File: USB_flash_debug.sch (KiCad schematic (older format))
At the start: 31 parts, among them IC2 TPS7A0518PDBVT, J6 E8124-015-01, J9 E8124-015-01, Q7 BSS138-7-F, Q8 BSS138-7-F, SW1 1X03, U13 FT232RQ-REEL, U9 FSUSB30UMX

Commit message: Routed USB flash and both USB connectors differential signals with tuning
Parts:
- removed U9: FSUSB30UMX, sc606-baseboard-footprints:UMLP-10_1.8x1.4mm, symbol sc606-baseboard:FSUSB30UMX
- added U9: FSUSB30MUX, antmicro-footprints:MSOP-10_W3mm, symbol antmicroInterfaceAnalogSwitchesSpecialPurpose:FSUSB30MUX
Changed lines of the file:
@@
 	14350 5500 14800 5500
-$Comp
-L sc606-baseboard:FSUSB30UMX U?
-U 1 1 62A45764
-P 2100 4650
-AR Path="/63348E64/62A45764" Ref="U?"  Part="1"
-AR Path="/61F60810/62A45764" Ref="U9"  Part="1"
-F 0 "U9" H 2050 5653 60  0000 C CNN
-F 1 "FSUSB30UMX" H 2050 5547 60  0000 C CNN
-F 2 "sc606-baseboard-footprints:UMLP-10_1.8x1.4mm" H 2250 4840 60  0001 L CNN
-F 3 "https://rocelec.widen.net/view/pdf/reufmpzzmy/ONSM-S-A0003587650-1.pdf?t.download=true&u=5oefqw" H 2250 4940 60  0001 L CNN
-F 4 "FSUSB30UMX" H 2250 5140 60  0001 L CNN "MPN"
-F 5 "ON SEMI" H 2270 5750 60  0001 L CNN "Manufacturer"
-	1    2100 4650
-	1    0    0    -1
-$EndComp
 $Comp
 L sc606-baseboard:E8124-015-01 J?
@@
 	1    0    0    -1
 $EndComp
+$Comp
+L antmicroInterfaceAnalogSwitchesSpecialPurpose:FSUSB30MUX U9
+U 1 1 6214D265
+P 2100 4650
+F 0 "U9" H 2050 5653 60  0000 C CNN
+F 1 "FSUSB30MUX" H 2050 5547 60  0000 C CNN
+F 2 "antmicro-footprints:MSOP-10_W3mm" H 2250 4840 60  0001 L CNN
+F 3 "" H 2250 4940 60  0001 L CNN
+F 4 "FSUSB30MUX" H 2250 5140 60  0001 L CNN "MPN"
+F 5 "ON SEMI" H 2270 5750 60  0001 L CNN "Manufacturer"
+	1    2100 4650
+	1    0    0    -1
+$EndComp

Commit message: Connected SIM, SD, SoM GNDs
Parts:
- U9: footprint antmicro-footprints:MSOP-10_W3mm -> sc606-baseboard-footprints:MSOP-10_W3mm; symbol antmicroInterfaceAnalogSwitchesSpecialPurpose:FSUSB30MUX -> sc606-baseboard:FSUSB30MUX
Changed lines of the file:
@@
 $EndComp
 $Comp
-L antmicroInterfaceAnalogSwitchesSpecialPurpose:FSUSB30MUX U9
+L sc606-baseboard:FSUSB30MUX U9
 U 1 1 6214D265
 P 2100 4650
 F 0 "U9" H 2050 5653 60  0000 C CNN
 F 1 "FSUSB30MUX" H 2050 5547 60  0000 C CNN
-F 2 "antmicro-footprints:MSOP-10_W3mm" H 2250 4840 60  0001 L CNN
+F 2 "sc606-baseboard-footprints:MSOP-10_W3mm" H 2250 4840 60  0001 L CNN
 F 3 "" H 2250 4940 60  0001 L CNN
 F 4 "FSUSB30MUX" H 2250 5140 60  0001 L CNN "MPN"

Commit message: All routes connected
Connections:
- net DEBUG_UART_TX: now also D23.1 (CH1), D23.10 (CH1); no longer D23.4 (CH3), D23.7 (CH3)
- new net: D23.4 (CH3), D23.7 (CH3)
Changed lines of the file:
@@
 Text GLabel 14250 5500 0    50   Input ~ 0
 DEBUG_UART_RX
-Text GLabel 14250 5400 0    50   Input ~ 0
+Text GLabel 14250 5200 0    50   Input ~ 0
 DEBUG_UART_TX
 Text GLabel 13900 4000 2    50   Input ~ 0
@@
 $EndComp
 Wire Wire Line
-	14250 5400 14450 5400
+	14250 5200 14450 5200
 Wire Wire Line
 	14250 5500 14350 5500
 Wire Wire Line
-	14450 4850 14450 5400
-Connection ~ 14450 5400
-Wire Wire Line
-	14450 5400 14800 5400
+	14450 4850 14450 5200
+Wire Wire Line
+	14450 5200 14800 5200
 Wire Wire Line
 	14350 4750 14350 5500
@@
 	1    0    0    -1
 $EndComp
+Connection ~ 14450 5200
 $EndSCHEMATC

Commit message: Cleaned/fixed USB flash debug sch
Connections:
- wire segments 115 -> 172
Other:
- note added: "SoM flashing and debug connectors"
- note added: "USB SoM flashing IF"
- note removed: "Micro USB flashing"
- moved on the sheet: C108, C109, C110, C111, C112, C113, C114, C115, C116, C117, C142, C143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

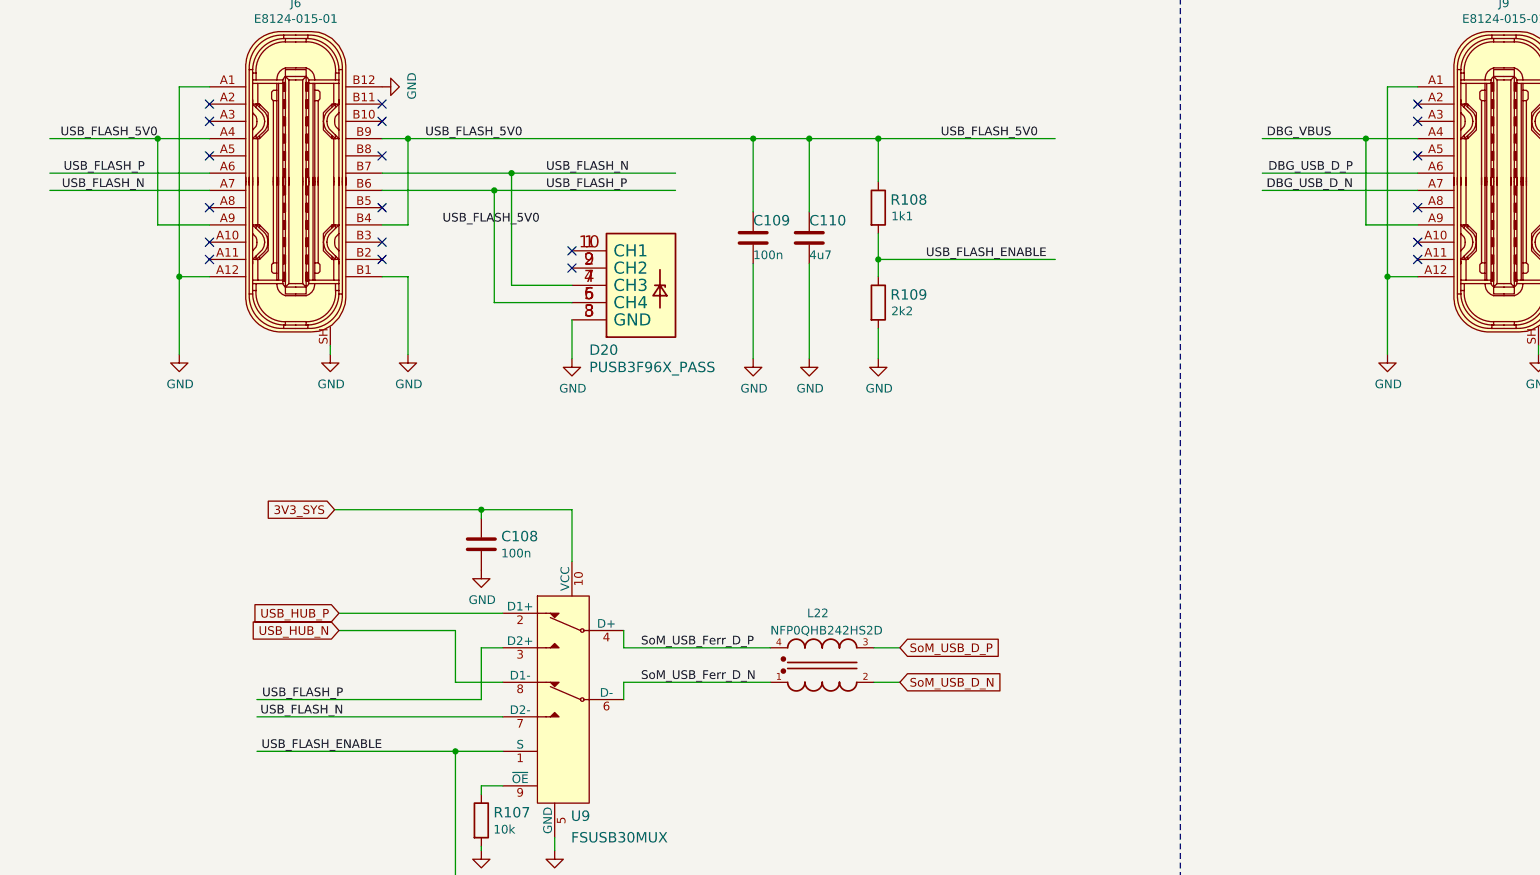
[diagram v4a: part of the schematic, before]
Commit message: Added schema for serial interface connectors
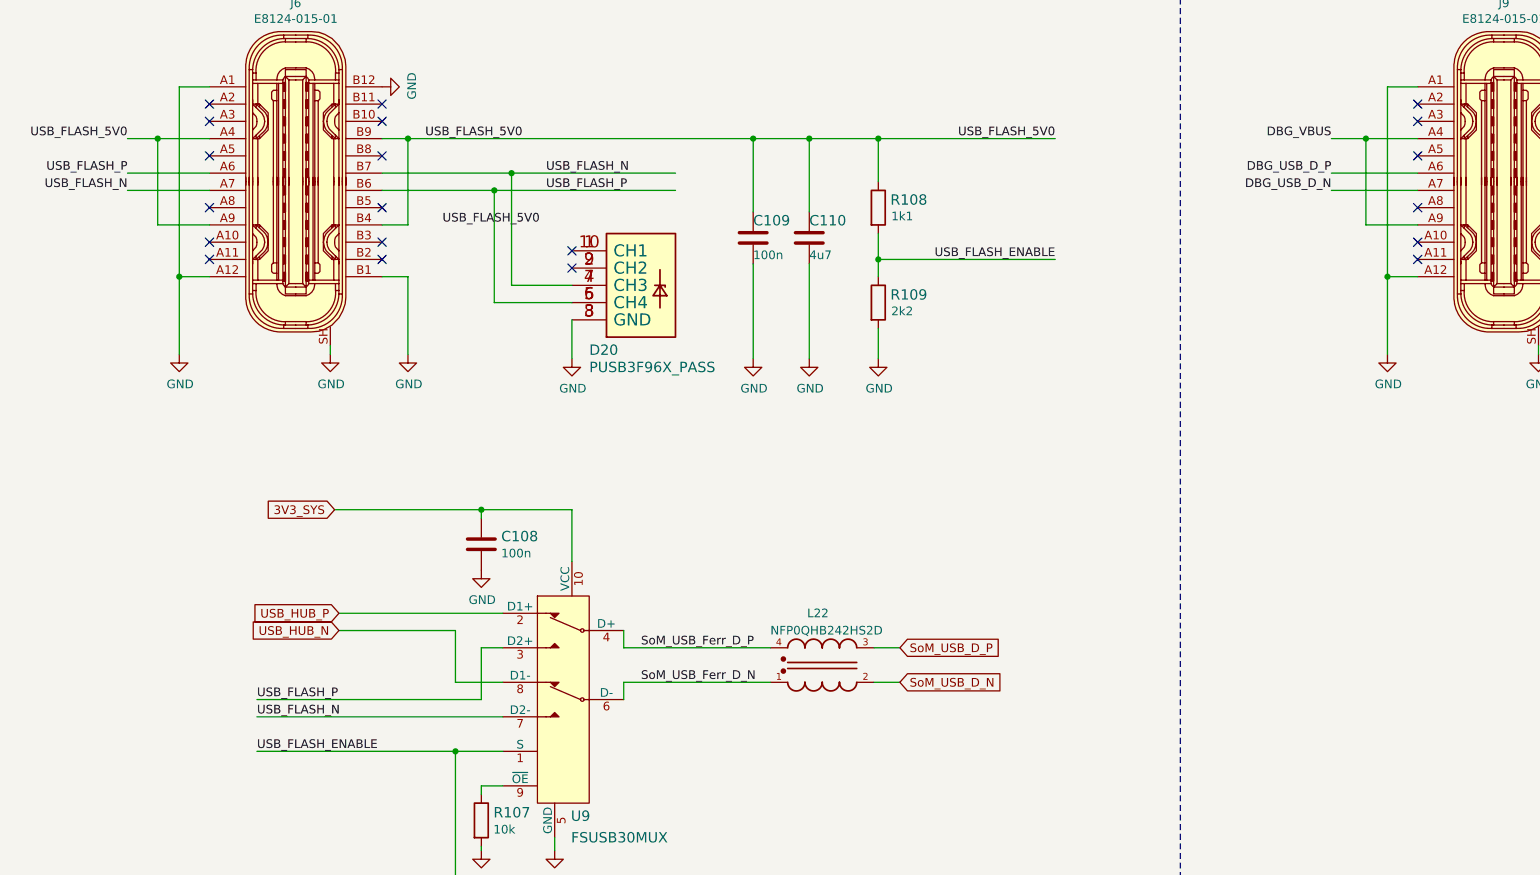
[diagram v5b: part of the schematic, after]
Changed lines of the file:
@@
 Text Label 3175 3575 0    50   ~ 0
 USB_FLASH_5V0
-Text Label 6725 3575 2    50   ~ 0
+Text Label 6825 3575 2    50   ~ 0
 USB_FLASH_5V0
 Text Label 10400 1750 0    50   ~ 0
@@
 	-1   0    0    -1
 $EndComp
-Text Label 8550 3775 2    50   ~ 0
+Text Label 8425 3775 2    50   ~ 0
 DBG_USB_D_P
-Text Label 8550 3875 2    50   ~ 0
+Text Label 8425 3875 2    50   ~ 0
 DBG_USB_D_N
 Wire Wire Line
-	8025 3875 8925 3875
-Wire Wire Line
-	8925 3775 8025 3775
+	8425 3875 8925 3875
+Wire Wire Line
+	8925 3775 8425 3775
 $Comp
 L sc606-baseboard:GND #PWR0173
@@
 	0    -1   -1   0
 $EndComp
-Text Label 1625 3575 2    50   ~ 0
+Text Label 1450 3575 2    50   ~ 0
 USB_FLASH_5V0
 Wire Wire Line
-	1000 3575 1625 3575
+	1450 3575 1625 3575
 NoConn ~ 4025 4225
 NoConn ~ 4025 4325
@@
 NoConn ~ 1925 3375
 Wire Wire Line
-	1925 3775 1000 3775
-Wire Wire Line
-	1000 3875 1925 3875
-Text Label 1550 3775 2    50   ~ 0
+	1925 3775 1450 3775
+Wire Wire Line
+	1450 3875 1925 3875
+Text Label 1450 3775 2    50   ~ 0
 USB_FLASH_P
-Text Label 1550 3875 2    50   ~ 0
+Text Label 1450 3875 2    50   ~ 0
 USB_FLASH_N
 $Comp
@@
 Text GLabel 2675 6325 0    50   Input ~ 0
 USB_HUB_P
-Text Label 6775 4275 2    50   ~ 0
+Text Label 6825 4275 2    50   ~ 0
 USB_FLASH_ENABLE
-Text Label 2925 7125 2    50   ~ 0
+Text Label 2200 7125 0    50   ~ 0
 USB_FLASH_ENABLE
-Text Label 2700 6925 2    50   ~ 0
-USB_FLASH_N
-Text Label 2700 6825 2    50   ~ 0
-USB_FLASH_P
 Wire Wire Line
 	2200 7125 3350 7125
@@
 	3075 3575 2925 3575
 $Comp
-L sc606-baseboard:GND #PWR?
+L sc606-baseboard:GND #PWR077
 U 1 1 6238159F
 P 5075 4850
-F 0 "#PWR?" H 5075 4600 50  0001 C CNN
+F 0 "#PWR077" H 5075 4600 50  0001 C CNN
 F 1 "GND" H 5080 4677 50  0000 C CNN
 F 2 "" H 5075 4850 50  0001 C CNN
@@
 	5075 4850 5075 4300
 $Comp
-L sc606-baseboard:GND #PWR?
+L sc606-baseboard:GND #PWR078
 U 1 1 62386BF6
 P 5400 4850
-F 0 "#PWR?" H 5400 4600 50  0001 C CNN
+F 0 "#PWR078" H 5400 4600 50  0001 C CNN
 F 1 "GND" H 5405 4677 50  0000 C CNN
 F 2 "" H 5400 4850 50  0001 C CNN
@@
 	3500 7675 3500 7700
 $Comp
-L sc606-baseboard:GND #PWR?
+L sc606-baseboard:GND #PWR048
 U 1 1 62503171
 P 3500 7700
-F 0 "#PWR?" H 3500 7450 50  0001 C CNN
+F 0 "#PWR048" H 3500 7450 50  0001 C CNN
 F 1 "GND" H 3505 7527 50  0000 C CNN
 F 2 "" H 3500 7700 50  0001 C CNN
@@
 	4200 8800 3925 8800
 $Comp
-L sc606-baseboard:GND #PWR?
+L sc606-baseboard:GND #PWR050
 U 1 1 625B110A
 P 4700 9900
-F 0 "#PWR?" H 4700 9650 50  0001 C CNN
+F 0 "#PWR050" H 4700 9650 50  0001 C CNN
 F 1 "GND" H 4705 9727 50  0000 C CNN
 F 2 "" H 4700 9900 50  0001 C CNN
@@
 	12250 1850 12250 2300
 $Comp
-L sc606-baseboard:GND #PWR?
+L sc606-baseboard:GND #PWR0128
 U 1 1 6265DDF7
 P 12250 2300
-F 0 "#PWR?" H 12250 2050 50  0001 C CNN
+F 0 "#PWR0128" H 12250 2050 50  0001 C CNN
 F 1 "GND" H 12255 2127 50  0000 C CNN
 F 2 "" H 12250 2300 50  0001 C CNN
@@
 DBG_VBUS
 $Comp
-L sc606-baseboard:GND #PWR?
+L sc606-baseboard:GND #PWR079
 U 1 1 62783B1B
 P 8750 4825
-F 0 "#PWR?" H 8750 4575 50  0001 C CNN
+F 0 "#PWR079" H 8750 4575 50  0001 C CNN
 F 1 "GND" H 8755 4652 50  0000 C CNN
 F 2 "" H 8750 4825 50  0001 C CNN
@@
 	8625 4075 8925 4075
 Wire Wire Line
-	8625 3575 8025 3575
+	8625 3575 8425 3575
 Connection ~ 8625 3575
 Wire Wire Line
 	8925 3275 8750 3275
 $Comp
-L sc606-baseboard:GND #PWR?
+L sc606-baseboard:GND #PWR080
 U 1 1 627E6EF7
 P 10075 4825
-F 0 "#PWR?" H 10075 4575 50  0001 C CNN
+F 0 "#PWR080" H 10075 4575 50  0001 C CNN
 F 1 "GND" H 10080 4652 50  0000 C CNN
 F 2 "" H 10075 4825 50  0001 C CNN
@@
 Connection ~ 10850 1750
 $Comp
-L sc606-baseboard:GND #PWR?
+L sc606-baseboard:GND #PWR0130
 U 1 1 6294152B
 P 12250 3525
-F 0 "#PWR?" H 12250 3275 50  0001 C CNN
+F 0 "#PWR0130" H 12250 3275 50  0001 C CNN
 F 1 "GND" H 12325 3375 50  0000 R CNN
 F 2 "" H 12250 3525 50  0001 C CNN
@@
 $EndComp
 $Comp
-L sc606-baseboard:GND #PWR?
+L sc606-baseboard:GND #PWR0116
 U 1 1 62B2179B
 P 11400 4825
-F 0 "#PWR?" H 11400 4575 50  0001 C CNN
+F 0 "#PWR0116" H 11400 4575 50  0001 C CNN
 F 1 "GND" H 11405 4652 50  0000 C CNN
 F 2 "" H 11400 4825 50  0001 C CNN
@@
 	11400 4825 11400 4675
 $Comp
-L sc606-baseboard:GND #PWR?
+L sc606-baseboard:GND #PWR0126
 U 1 1 62B3034F
 P 11700 4825
-F 0 "#PWR?" H 11700 4575 50  0001 C CNN
+F 0 "#PWR0126" H 11700 4575 50  0001 C CNN
 F 1 "GND" H 11705 4652 50  0000 C CNN
 F 2 "" H 11700 4825 50  0001 C CNN
@@
 	11700 4825 11700 4675
 $Comp
-L sc606-baseboard:GND #PWR?
+L sc606-baseboard:GND #PWR0134
 U 1 1 62B36C20
 P 12400 4825
-F 0 "#PWR?" H 12400 4575 50  0001 C CNN
+F 0 "#PWR0134" H 12400 4575 50  0001 C CNN
 F 1 "GND" H 12405 4652 50  0000 C CNN
 F 2 "" H 12400 4825 50  0001 C CNN
@@
 	11400 3500 11400 3475
 $Comp
-L sc606-baseboard:GND #PWR?
+L sc606-baseboard:GND #PWR099
 U 1 1 62BB0F6C
 P 11400 3500
-F 0 "#PWR?" H 11400 3250 50  0001 C CNN
+F 0 "#PWR099" H 11400 3250 50  0001 C CNN
 F 1 "GND" H 11405 3327 50  0000 C CNN
 F 2 "" H 11400 3500 50  0001 C CNN
@@
 	11700 3500 11700 3475
 $Comp
-L sc606-baseboard:GND #PWR?
+L sc606-baseboard:GND #PWR0121
 U 1 1 62BAA1F8
 P 11700 3500
-F 0 "#PWR?" H 11700 3250 50  0001 C CNN
+F 0 "#PWR0121" H 11700 3250 50  0001 C CNN
 F 1 "GND" H 11705 3327 50  0000 C CNN
 F 2 "" H 11700 3500 50  0001 C CNN
@@
 	12500 3075 14650 3075
 $Comp
-L sc606-baseboard:GND #PWR?
+L sc606-baseboard:GND #PWR0135
 U 1 1 62D346FE
 P 13875 4800
-F 0 "#PWR?" H 13875 4550 50  0001 C CNN
+F 0 "#PWR0135" H 13875 4550 50  0001 C CNN
 F 1 "GND" H 13880 4627 50  0000 C CNN
 F 2 "" H 13875 4800 50  0001 C CNN
@@
 Wire Wire Line
 	14525 3775 13575 3775
+Text Label 2200 6925 0    50   ~ 0
+USB_FLASH_N
+Text Label 2200 6825 0    50   ~ 0
+USB_FLASH_P
 $EndSCHEMATC

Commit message: Schematic cleanup
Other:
- note added: "info: UART lines crossed\nfrom SoM side"
- note removed: "info: crossed from SoM"
- moved on the sheet: C112, C142
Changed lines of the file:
@@
 Text GLabel 14775 3075 2    50   Input ~ 0
 DEBUG_UART_TX
-Text Notes 14575 3925 0    50   ~ 0
-info: crossed from SoM
+Text Notes 14750 3500 0    50   ~ 0
+info: UART lines crossed\nfrom SoM side
 Wire Wire Line
 	14775 3775 14525 3775
@@
 U 1 1 6319E602
 P 13875 4500
-F 0 "C117" H 13875 4600 60  0000 L CNN
+F 0 "C117" H 13990 4455 60  0000 L CNN
 F 1 "C_100n_0402" H 13875 4350 60  0001 C CNN
 F 2 "sc606-baseboard-footprints:0402-cap" H 14075 4700 60  0001 L CNN
@@
 F 4 "Murata" H 14075 4900 60  0001 L CNN "Manufacturer"
 F 5 "GRM155R61H104KE14D" H 14075 4800 60  0001 L CNN "MPN"
-F 6 "100n" H 13875 4400 50  0000 L CNN "Val"
+F 6 "100n" H 13990 4553 50  0000 L CNN "Val"
 	1    13875 4500
 	1    0    0    1
@@
 	11700 4275 12575 4275
 Wire Wire Line
-	11400 4375 11400 4175
-Wire Wire Line
-	11400 4175 12575 4175
+	11500 4375 11500 4175
+Wire Wire Line
+	11500 4175 12575 4175
 Connection ~ 11700 4275
-Connection ~ 11400 4175
+Connection ~ 11500 4175
 Text Label 10225 3875 0    50   ~ 0
 DBG_USB_D_P
@@
 	-1   0    0    -1
 $EndComp
-Text Label 8425 3775 2    50   ~ 0
+Text Label 8050 3775 0    50   ~ 0
 DBG_USB_D_P
-Text Label 8425 3875 2    50   ~ 0
+Text Label 8050 3875 0    50   ~ 0
 DBG_USB_D_N
 Wire Wire Line
-	8425 3875 8925 3875
-Wire Wire Line
-	8925 3775 8425 3775
+	8050 3875 8925 3875
+Wire Wire Line
+	8925 3775 8050 3775
 $Comp
 L sc606-baseboard:GND #PWR0173
@@
 Wire Wire Line
 	6825 3575 5800 3575
-Text Label 3275 4075 0    50   ~ 0
-USB_FLASH_5V0
 $Comp
 L sc606-baseboard:GND #PWR0167
@@
 Wire Wire Line
 	8925 3575 8625 3575
-Text Label 8425 3575 2    50   ~ 0
+Text Label 8050 3575 0    50   ~ 0
 DBG_VBUS
 $Comp
@@
 	8625 4075 8925 4075
 Wire Wire Line
-	8625 3575 8425 3575
+	8625 3575 8050 3575
 Connection ~ 8625 3575
 Wire Wire Line
@@
 	13075 1750 13075 3175
 Wire Wire Line
-	11400 4175 11400 3875
+	11500 4175 11500 3875
 Wire Wire Line
 	9925 3875 10875 3875
@@
 L sc606-baseboard:C_47p_0402 C112
 U 1 1 61FF90E8
-P 11400 4525
-F 0 "C112" H 11450 4625 60  0000 L CNN
-F 1 "C_47p_0402" H 11400 4375 60  0001 C CNN
-F 2 "sc606-baseboard-footprints:0402-cap" H 11600 4725 60  0001 L CNN
-F 3 "" H 11400 4525 50  0001 C CNN
-F 4 "KEMET" H 11600 4925 60  0001 L CNN "Manufacturer"
-F 5 "C0402C470J5GACTU" H 11600 4825 60  0001 L CNN "MPN"
-F 6 "47p" H 11450 4425 50  0000 L CNN "Val"
-	1    11400 4525
+P 11500 4525
+F 0 "C112" H 11386 4570 60  0000 R CNN
+F 1 "C_47p_0402" H 11500 4375 60  0001 C CNN
+F 2 "sc606-baseboard-footprints:0402-cap" H 11700 4725 60  0001 L CNN
+F 3 "" H 11500 4525 50  0001 C CNN
+F 4 "KEMET" H 11700 4925 60  0001 L CNN "Manufacturer"
+F 5 "C0402C470J5GACTU" H 11700 4825 60  0001 L CNN "MPN"
+F 6 "47p" H 11386 4472 50  0000 R CNN "Val"
+	1    11500 4525
 	1    0    0    -1
 $EndComp
@@
 U 1 1 61FF8CD9
 P 11700 4525
-F 0 "C114" H 11750 4625 60  0000 L CNN
+F 0 "C114" H 11815 4570 60  0000 L CNN
 F 1 "C_47p_0402" H 11700 4375 60  0001 C CNN
 F 2 "sc606-baseboard-footprints:0402-cap" H 11900 4725 60  0001 L CNN
@@
 F 4 "KEMET" H 11900 4925 60  0001 L CNN "Manufacturer"
 F 5 "C0402C470J5GACTU" H 11900 4825 60  0001 L CNN "MPN"
-F 6 "47p" H 11750 4425 50  0000 L CNN "Val"
+F 6 "47p" H 11815 4472 50  0000 L CNN "Val"
 	1    11700 4525
 	1    0    0    -1
@@
 L sc606-baseboard:GND #PWR0116
 U 1 1 62B2179B
-P 11400 4825
-F 0 "#PWR0116" H 11400 4575 50  0001 C CNN
-F 1 "GND" H 11405 4652 50  0000 C CNN
-F 2 "" H 11400 4825 50  0001 C CNN
-F 3 "" H 11400 4825 50  0001 C CNN
-	1    11400 4825
-	1    0    0    -1
-$EndComp
-Wire Wire Line
-	11400 4825 11400 4675
+P 11500 4825
+F 0 "#PWR0116" H 11500 4575 50  0001 C CNN
+F 1 "GND" H 11505 4652 50  0000 C CNN
+F 2 "" H 11500 4825 50  0001 C CNN
+F 3 "" H 11500 4825 50  0001 C CNN
+	1    11500 4825
+	1    0    0    -1
+$EndComp
+Wire Wire Line
+	11500 4825 11500 4675
 $Comp
 L sc606-baseboard:GND #PWR0126
@@
 $EndComp
 Wire Wire Line
-	11700 3500 11700 3475
+	11625 3500 11625 3475
 $Comp
 L sc606-baseboard:GND #PWR0121
 U 1 1 62BAA1F8
-P 11700 3500
-F 0 "#PWR0121" H 11700 3250 50  0001 C CNN
-F 1 "GND" H 11705 3327 50  0000 C CNN
-F 2 "" H 11700 3500 50  0001 C CNN
-F 3 "" H 11700 3500 50  0001 C CNN
-	1    11700 3500
+P 11625 3500
+F 0 "#PWR0121" H 11625 3250 50  0001 C CNN
+F 1 "GND" H 11630 3327 50  0000 C CNN
+F 2 "" H 11625 3500 50  0001 C CNN
+F 3 "" H 11625 3500 50  0001 C CNN
+	1    11625 3500
 	1    0    0    -1
 $EndComp
@@
 U 1 1 621A2299
 P 11400 3325
-F 0 "C143" H 11400 3425 60  0000 L CNN
+F 0 "C143" H 11286 3370 60  0000 R CNN
 F 1 "C_4u7_0402" H 11400 3175 60  0001 C CNN
 F 2 "sc606-baseboard-footprints:0402-cap" H 11600 3525 60  0001 L CNN
@@
 F 4 "MURATA" H 11600 3725 60  0001 L CNN "Manufacturer"
 F 5 "GRM155R61A475MEAAD" H 11600 3625 60  0001 L CNN "MPN"
-F 6 "4u7" H 11400 3225 50  0000 L CNN "Val"
+F 6 "4u7" H 11286 3272 50  0000 R CNN "Val"
 	1    11400 3325
 	1    0    0    -1
@@
 L sc606-baseboard:C_100n_0402 C142
 U 1 1 621A2290
-P 11700 3325
-F 0 "C142" H 11700 3425 60  0000 L CNN
-F 1 "C_100n_0402" H 11700 3175 60  0001 C CNN
-F 2 "sc606-baseboard-footprints:0402-cap" H 11900 3525 60  0001 L CNN
-F 3 "" H 11700 3325 50  0001 C CNN
-F 4 "Murata" H 11900 3725 60  0001 L CNN "Manufacturer"
-F 5 "GRM155R61H104KE14D" H 11900 3625 60  0001 L CNN "MPN"
-F 6 "100n" H 11700 3225 50  0000 L CNN "Val"
-	1    11700 3325
+P 11625 3325
+F 0 "C142" H 11740 3370 60  0000 L CNN
+F 1 "C_100n_0402" H 11625 3175 60  0001 C CNN
+F 2 "sc606-baseboard-footprints:0402-cap" H 11825 3525 60  0001 L CNN
+F 3 "" H 11625 3325 50  0001 C CNN
+F 4 "Murata" H 11825 3725 60  0001 L CNN "Manufacturer"
+F 5 "GRM155R61H104KE14D" H 11825 3625 60  0001 L CNN "MPN"
+F 6 "100n" H 11740 3272 50  0000 L CNN "Val"
+	1    11625 3325
 	1    0    0    -1
 $EndComp
@@
 Connection ~ 10875 3875
 Wire Wire Line
-	10875 3875 11400 3875
+	10875 3875 11500 3875
 Wire Wire Line
 	10075 4375 10575 4375
@@
 	10850 3075 11400 3075
 Wire Wire Line
-	11700 3075 11700 3175
+	11625 3075 11625 3175
 Connection ~ 10850 3075
 Wire Wire Line
@@
 Connection ~ 11400 3075
 Wire Wire Line
-	11400 3075 11700 3075
+	11400 3075 11625 3075
 Wire Wire Line
 	13175 2575 12250 2575
